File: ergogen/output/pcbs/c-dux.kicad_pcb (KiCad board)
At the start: 2 copper layers, 147.3 x 116.9 mm, 25 parts, among them SW1 SW_Push_Lock, SW2 SW-SMD_4P

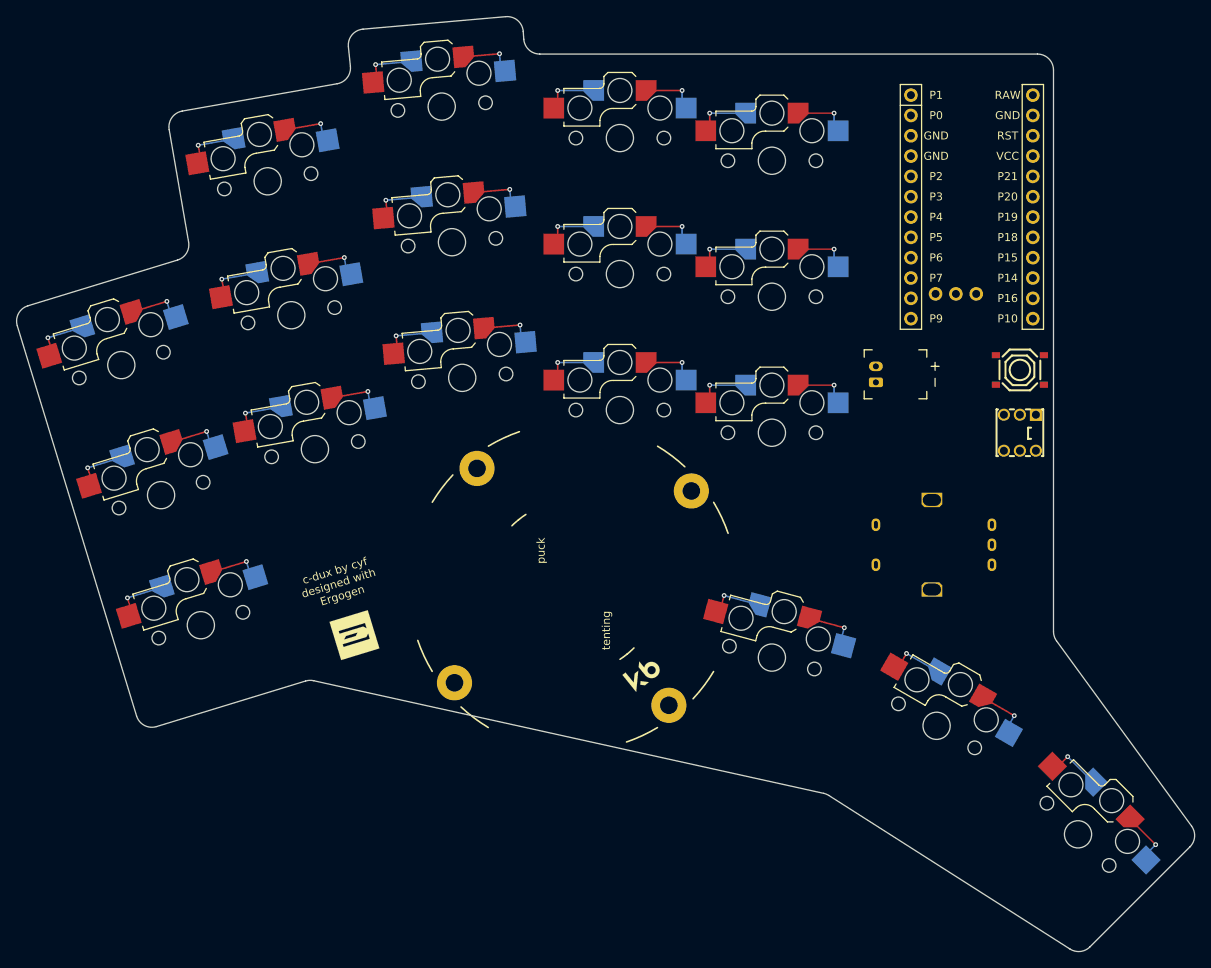
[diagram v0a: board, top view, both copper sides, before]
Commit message: kicad: update ergogen generated pcb.
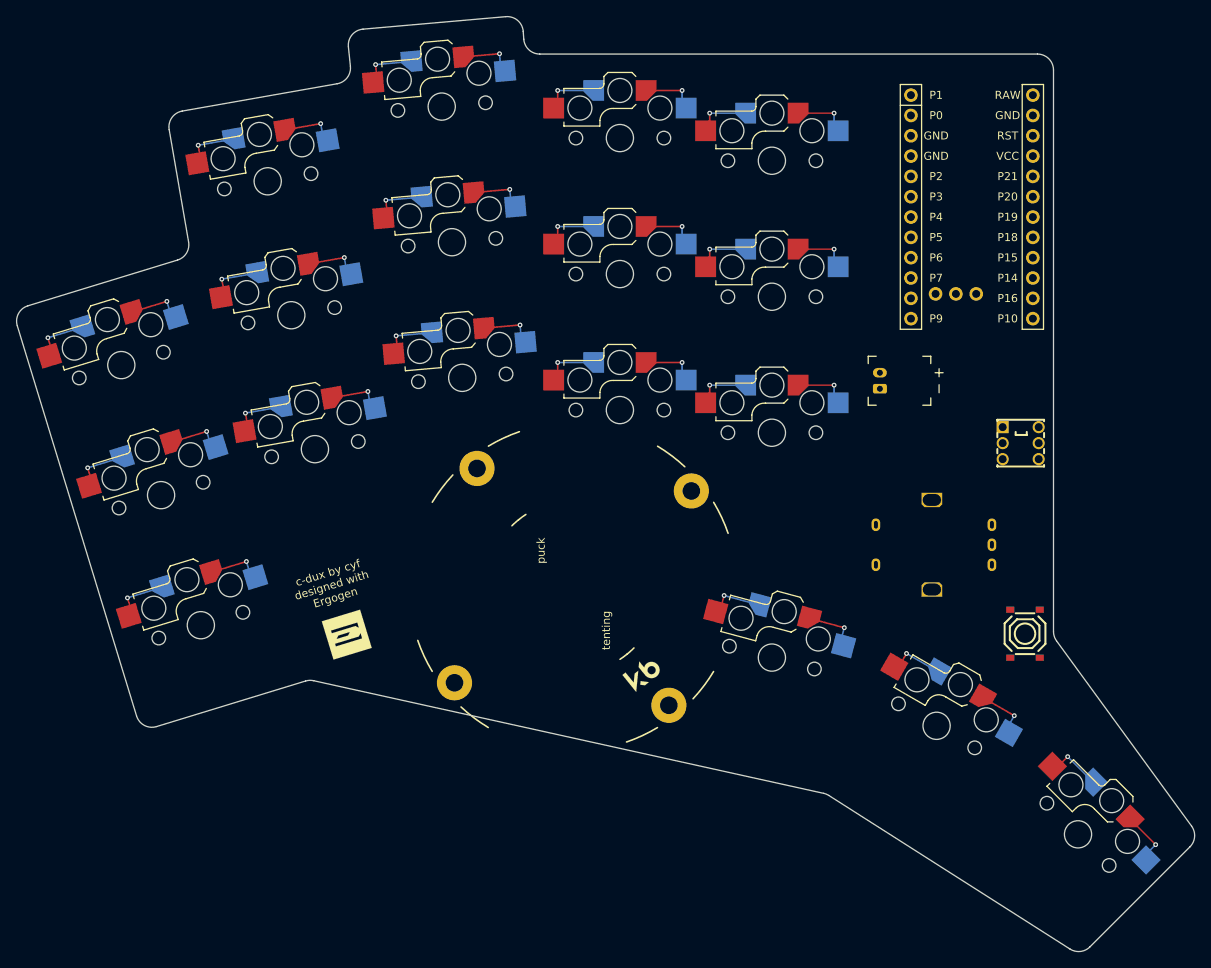
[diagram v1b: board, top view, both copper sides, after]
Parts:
- moved SW2 33.0 mm to (248.1, 151.8), turned to 270 degrees
- moved SW1 1.30 mm to (247.5, 128.0), turned to 90 degrees
- moved LOGO1 0.96 mm to (163.3, 151.9)
- moved JST1 0.94 mm to (229.9, 120.2)
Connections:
- S1 pad 1: P102 -> GND
- S10 pad 1: P8 -> GND
- S11 pad 1: P5 -> GND
- S12 pad 1: P20 -> GND
- S13 pad 1: P9 -> GND
- S14 pad 1: P6 -> GND
- S15 pad 1: P19 -> GND
- S16 pad 1: P107 -> GND
- S17 pad 1: P15 -> GND
- S18 pad 1: P14 -> GND
- S2 pad 1: P2 -> GND
- S3 pad 1: P0 -> GND
- S4 pad 1: P101 -> GND
- S5 pad 1: P3 -> GND
- S6 pad 1: P1 -> GND
- S7 pad 1: P7 -> GND
- S8 pad 1: P4 -> GND
- S9 pad 1: P21 -> GND
- SW2 pad 1: RST -> GND
- SW2 pad 3: GND -> RST
